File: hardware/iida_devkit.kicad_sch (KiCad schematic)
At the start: 7 parts

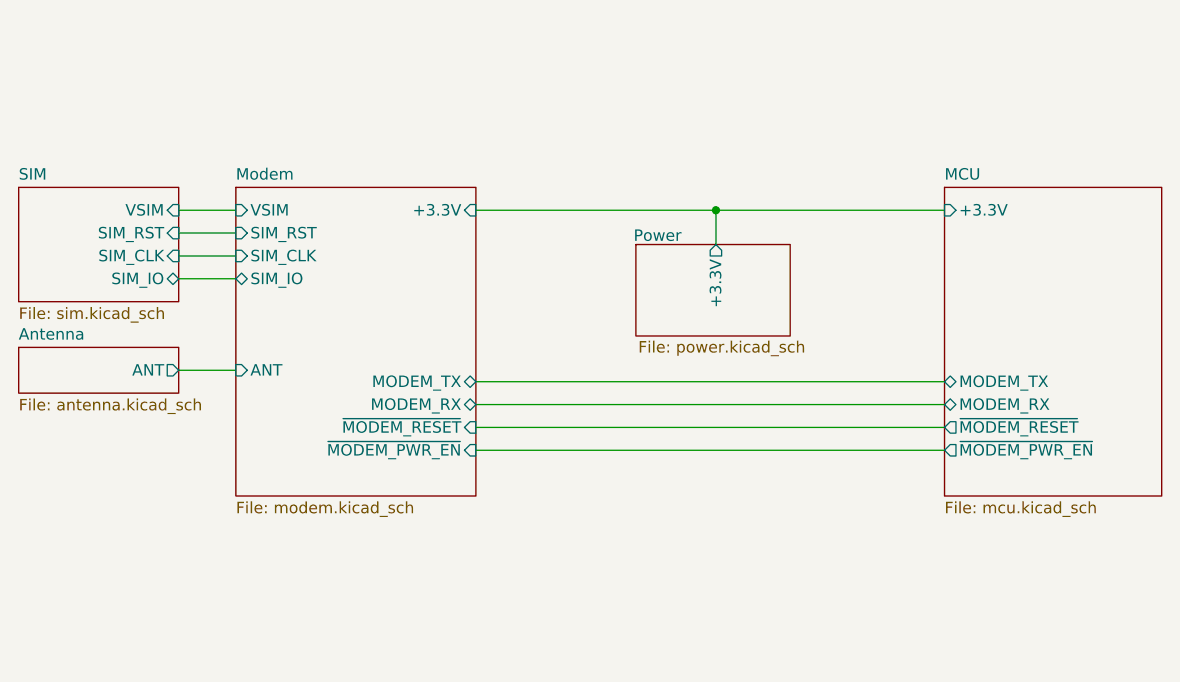
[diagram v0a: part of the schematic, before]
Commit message: HW: Cleanup schematic
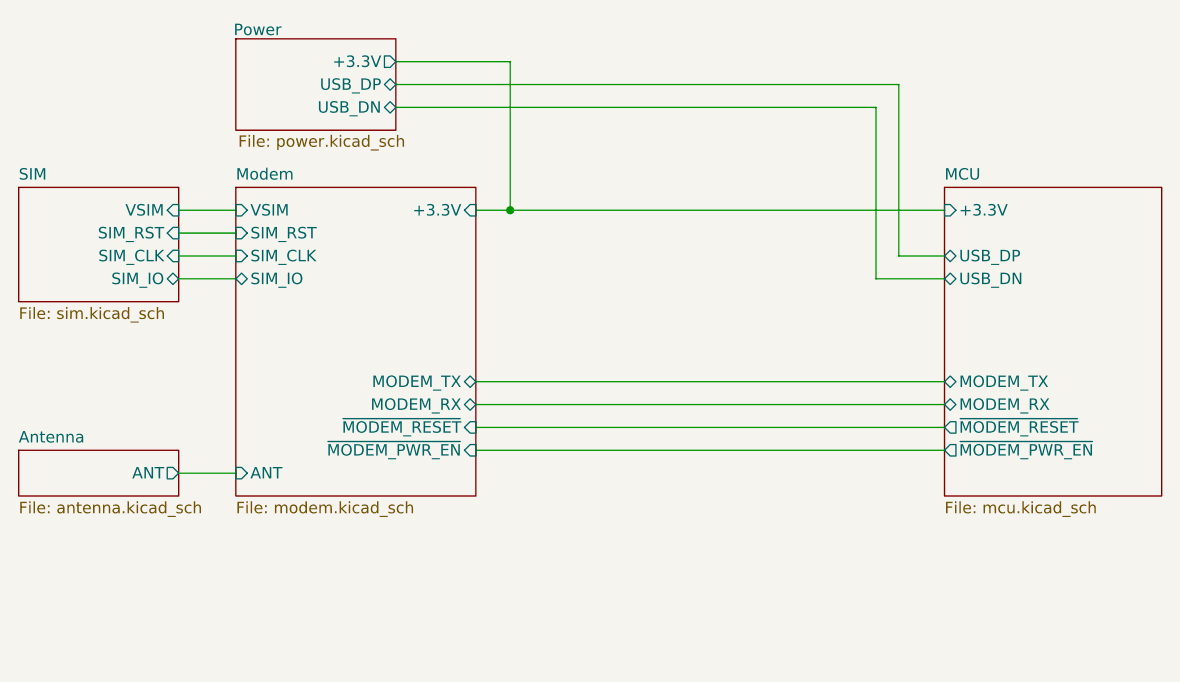
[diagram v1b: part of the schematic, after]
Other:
- sheet MCU ports: added USB_DN, USB_DP; removed none
- sheet Power ports: added USB_DN, USB_DP; removed none
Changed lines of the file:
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@@
-	)
-	(junction
-		(at 152.4 83.82)
-		(diameter 0)
-		(color 0 0 0 0)
 	)
 	(junction
@@
 	)
 	(junction
+		(at 129.54 83.82)
+		(diameter 0)
+		(color 0 0 0 0)
+	)
+	(junction
 		(at 137.16 189.23)
 		(diameter 0)
@@
 	(wire
 		(pts
-			(xy 152.4 83.82) (xy 152.4 87.63)
+			(xy 129.54 67.31) (xy 129.54 83.82)
 		)
 		(stroke
@@
 	(wire
 		(pts
+			(xy 170.18 91.44) (xy 177.8 91.44)
+		)
+		(stroke
+			(width 0)
+			(type default)
+		)
+	)
+	(wire
+		(pts
 			(xy 92.71 86.36) (xy 99.06 86.36)
 		)
@@
 	(wire
 		(pts
-			(xy 152.4 83.82) (xy 177.8 83.82)
+			(xy 172.72 69.85) (xy 116.84 69.85)
 		)
 		(stroke
@@
 	(wire
 		(pts
-			(xy 125.73 83.82) (xy 152.4 83.82)
+			(xy 116.84 67.31) (xy 129.54 67.31)
+		)
+		(stroke
+			(width 0)
+			(type default)
+		)
+	)
+	(wire
+		(pts
+			(xy 125.73 83.82) (xy 129.54 83.82)
 		)
 		(stroke
@@
 	(wire
 		(pts
-			(xy 92.71 101.6) (xy 99.06 101.6)
+			(xy 170.18 72.39) (xy 170.18 91.44)
+		)
+		(stroke
+			(width 0)
+			(type default)
+		)
+	)
+	(wire
+		(pts
+			(xy 92.71 113.03) (xy 99.06 113.03)
+		)
+		(stroke
+			(width 0)
+			(type default)
+		)
+	)
+	(wire
+		(pts
+			(xy 177.8 88.9) (xy 172.72 88.9)
+		)
+		(stroke
+			(width 0)
+			(type default)
+		)
+	)
+	(wire
+		(pts
+			(xy 172.72 88.9) (xy 172.72 69.85)
+		)
+		(stroke
+			(width 0)
+			(type default)
+		)
+	)
+	(wire
+		(pts
+			(xy 116.84 72.39) (xy 170.18 72.39)
+		)
+		(stroke
+			(width 0)
+			(type default)
+		)
+	)
+	(wire
+		(pts
+			(xy 129.54 83.82) (xy 177.8 83.82)
 		)
 		(stroke
@@
 		)
 		(pin "ANT" input
-			(at 99.06 101.6 180)
-			(effects
-				(font
-					(size 1.27 1.27)
+			(at 99.06 113.03 180)
+			(effects
+				(font
+					(size 1.27 1.27)
+					(color 0 0 0 1)
 				)
 				(justify left)
@@
 			)
 		)
+		(pin "USB_DP" bidirectional
+			(at 177.8 88.9 180)
+			(effects
+				(font
+					(size 1.27 1.27)
+				)
+				(justify left)
+			)
+		)
+		(pin "USB_DN" bidirectional
+			(at 177.8 91.44 180)
+			(effects
+				(font
+					(size 1.27 1.27)
+				)
+				(justify left)
+			)
+		)
 		(instances
 			(project "iida_devkit"
@@
 	)
 	(sheet
-		(at 74.93 99.06)
+		(at 74.93 110.49)
 		(size 17.78 5.08)
 		(fields_autoplaced yes)
@@
 		)
 		(property "Sheetname" "Antenna"
-			(at 74.93 98.3484 0)
+			(at 74.93 109.7784 0)
 			(effects
 				(font
@@
 		)
 		(property "Sheetfile" "antenna.kicad_sch"
-			(at 74.93 104.7246 0)
+			(at 74.93 116.1546 0)
 			(effects
 				(font
@@
 		)
 		(pin "ANT" output
-			(at 92.71 101.6 0)
-			(effects
-				(font
-					(size 1.27 1.27)
+			(at 92.71 113.03 0)
+			(effects
+				(font
+					(size 1.27 1.27)
+					(color 0 0 0 1)
 				)
 				(justify right)
@@
 	)
 	(sheet
-		(at 143.51 87.63)
-		(size 17.145 10.16)
+		(at 99.06 64.77)
+		(size 17.78 10.16)
 		(stroke
 			(width 0.1524)
@@
 		)
 		(property "Sheetname" "Power"
-			(at 143.256 87.376 0)
+			(at 98.806 64.516 0)
 			(effects
 				(font
@@
 		)
 		(property "Sheetfile" "power.kicad_sch"
-			(at 143.764 98.298 0)
+			(at 99.314 75.438 0)
 			(effects
 				(font
@@
 		)
 		(pin "+3.3V" output
-			(at 152.4 87.63 90)
-			(effects
-				(font
+			(at 116.84 67.31 0)
+			(effects
+				(font
+					(size 1.27 1.27)
+				)
+				(justify right)
+			)
+		)
+		(pin "USB_DP" bidirectional
+			(at 116.84 69.85 0)
+			(effects
+				(font
+					(size 1.27 1.27)
+				)
+				(justify right)
+			)
+		)
+		(pin "USB_DN" bidirectional
+			(at 116.84 72.39 0)
+			(effects
+				(font

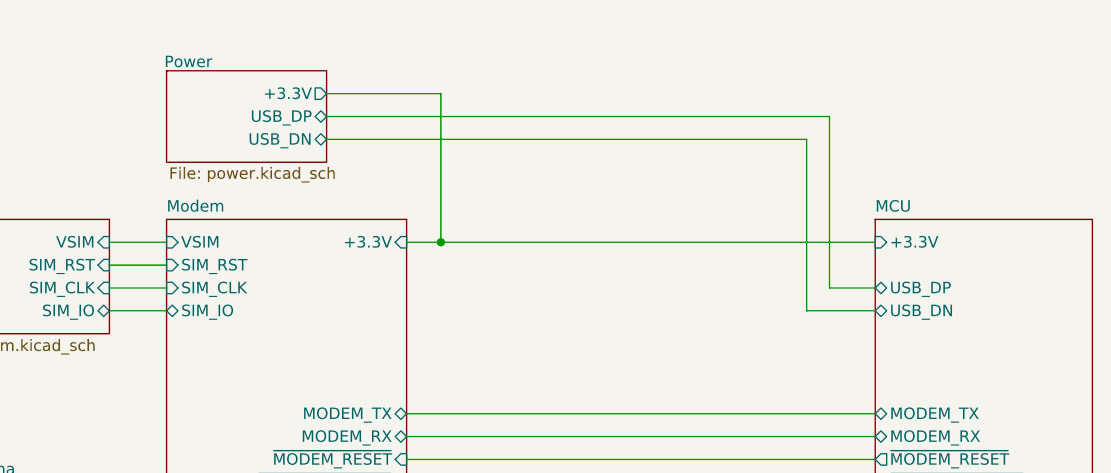
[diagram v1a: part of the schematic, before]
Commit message: HW: Connect +BATT to MCU
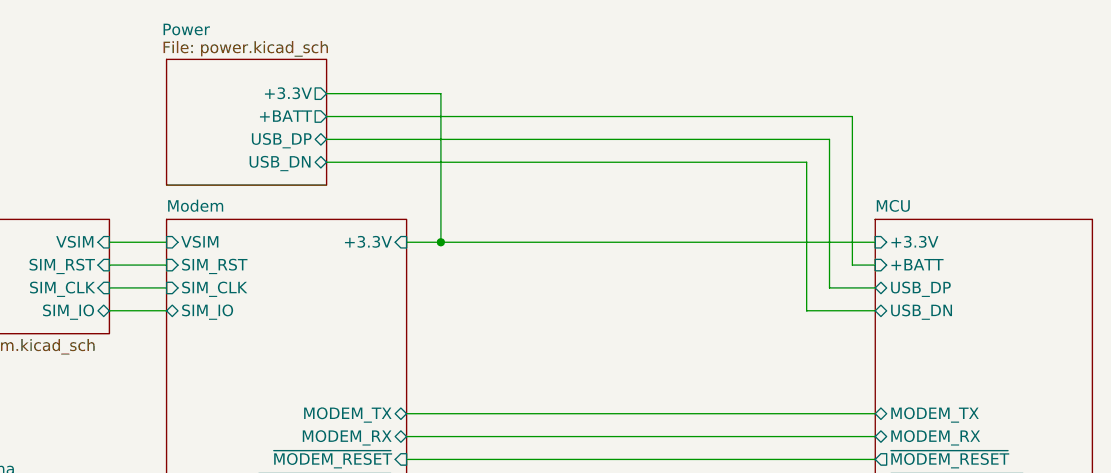
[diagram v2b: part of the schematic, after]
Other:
- sheet MCU ports: added +BATT; removed none
- sheet Power ports: added +BATT; removed none
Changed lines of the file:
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@@
 	(title_block
 		(title "Iida devkit")
-		(date "2024-09-22")
-		(rev "v4.1.0")
+		(date "2024-09-25")
+		(rev "v4.2.0")
 	)
 	(junction
@@
 	(wire
 		(pts
+			(xy 177.8 86.36) (xy 175.26 86.36)
+		)
+		(stroke
+			(width 0)
+			(type default)
+		)
+	)
+	(wire
+		(pts
+			(xy 175.26 69.85) (xy 116.84 69.85)
+		)
+		(stroke
+			(width 0)
+			(type default)
+		)
+	)
+	(wire
+		(pts
 			(xy 92.71 86.36) (xy 99.06 86.36)
 		)
@@
 	(wire
 		(pts
-			(xy 172.72 69.85) (xy 116.84 69.85)
+			(xy 172.72 72.39) (xy 116.84 72.39)
 		)
 		(stroke
@@
 	(wire
 		(pts
-			(xy 170.18 72.39) (xy 170.18 91.44)
+			(xy 170.18 74.93) (xy 170.18 91.44)
 		)
 		(stroke
@@
 	(wire
 		(pts
-			(xy 172.72 88.9) (xy 172.72 69.85)
-		)
-		(stroke
-			(width 0)
-			(type default)
-		)
-	)
-	(wire
-		(pts
-			(xy 116.84 72.39) (xy 170.18 72.39)
+			(xy 172.72 88.9) (xy 172.72 72.39)
+		)
+		(stroke
+			(width 0)
+			(type default)
+		)
+	)
+	(wire
+		(pts
+			(xy 116.84 74.93) (xy 170.18 74.93)
 		)
 		(stroke
@@
 		(pts
 			(xy 129.54 83.82) (xy 177.8 83.82)
+		)
+		(stroke
+			(width 0)
+			(type default)
+		)
+	)
+	(wire
+		(pts
+			(xy 175.26 86.36) (xy 175.26 69.85)
 		)
 		(stroke
@@
 			)
 		)
+		(pin "+BATT" input
+			(at 177.8 86.36 180)
+			(effects
+				(font
+					(size 1.27 1.27)
+				)
+				(justify left)
+			)
+		)
 		(instances
 			(project "iida_devkit"
@@
 	)
 	(sheet
-		(at 99.06 64.77)
-		(size 17.78 10.16)
+		(at 99.06 63.5)
+		(size 17.78 13.97)
 		(stroke
 			(width 0.1524)
@@
 		)
 		(property "Sheetname" "Power"
-			(at 98.806 64.516 0)
+			(at 98.552 60.96 0)
 			(effects
 				(font
@@
 		)
 		(property "Sheetfile" "power.kicad_sch"
-			(at 99.314 75.438 0)
+			(at 98.552 61.468 0)
 			(effects
 				(font
@@
 		)
 		(pin "USB_DP" bidirectional
+			(at 116.84 72.39 0)
+			(effects
+				(font
+					(size 1.27 1.27)
+				)
+				(justify right)
+			)
+		)
+		(pin "USB_DN" bidirectional
+			(at 116.84 74.93 0)
+			(effects
+				(font
+					(size 1.27 1.27)
+				)
+				(justify right)
+			)
+		)
+		(pin "+BATT" output
 			(at 116.84 69.85 0)
 			(effects
 				(font
-					(size 1.27 1.27)
-				)
-				(justify right)
-			)
-		)
-		(pin "USB_DN" bidirectional
-			(at 116.84 72.39 0)
-			(effects
-				(font

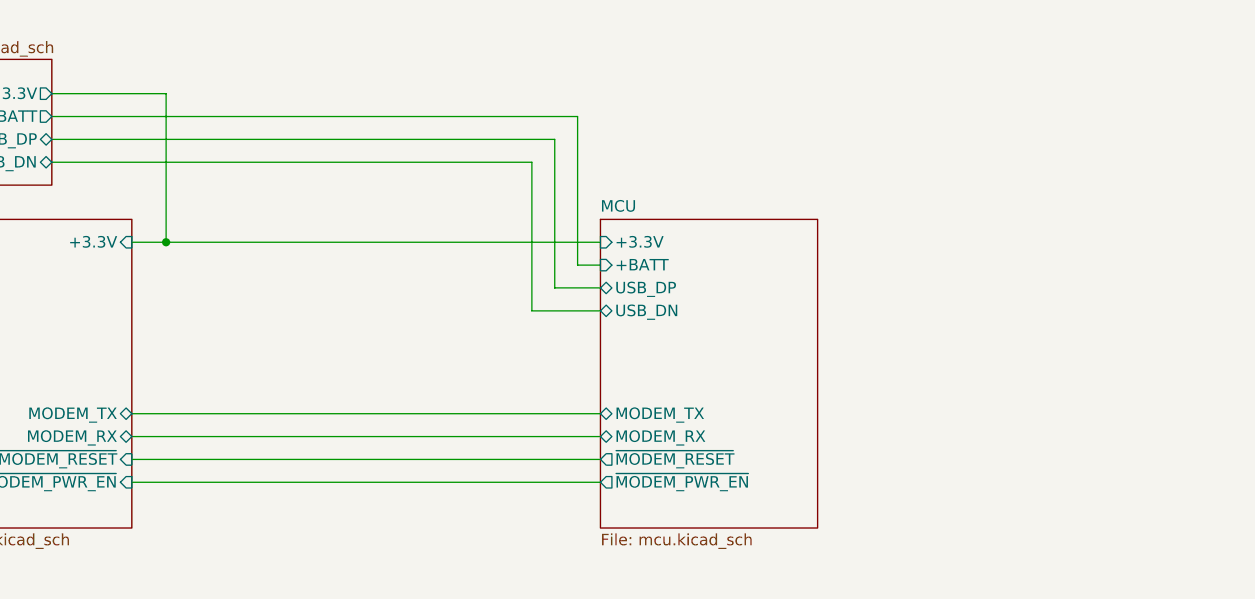
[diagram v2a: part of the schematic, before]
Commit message: HW: Improve thermals, silkscreen and schematic
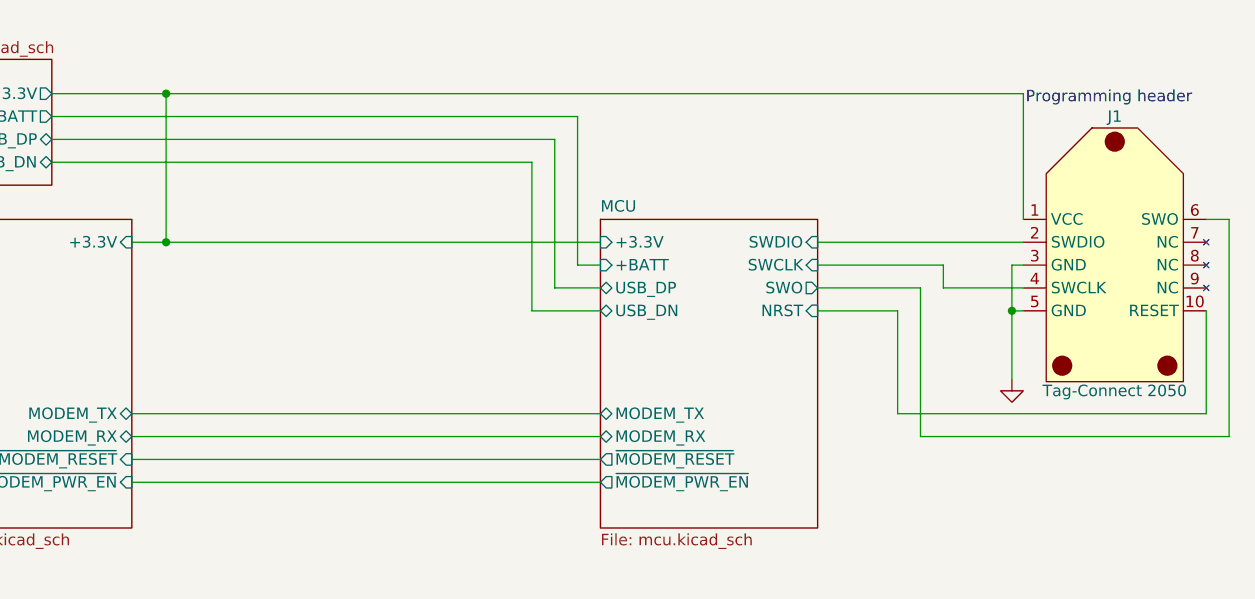
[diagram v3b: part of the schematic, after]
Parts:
- added J1: Tag-Connect 2050, Connector:Tag-Connect_TC2050-IDC-FP_2x05_P1.27mm_Vertical, symbol Tag-Connect:TC2050
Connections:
- net GND: now also J1.3 (GND), J1.5 (GND)
- net MCU/+3.3V: now also J1.1 (VCC)
- new net MCU/NRST: J1.10 (RESET)
- new net MCU/SWCLK: J1.4 (SWCLK)
- new net MCU/SWDIO: J1.2 (SWDIO)
- new net MCU/SWO: J1.6 (SWO)
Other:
- sheet MCU ports: added NRST, SWCLK, SWDIO, SWO; removed none
- note added: "Programming header"
